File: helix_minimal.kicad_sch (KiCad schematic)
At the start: 18 parts, among them J1 USB-C, J2 WIZ850io J1, J3 WIZ850io J2, J4 3V3 microSD SPI breakout, J5 SWD, U1 STM32C071FBP6, U2 AP2112K-3.3

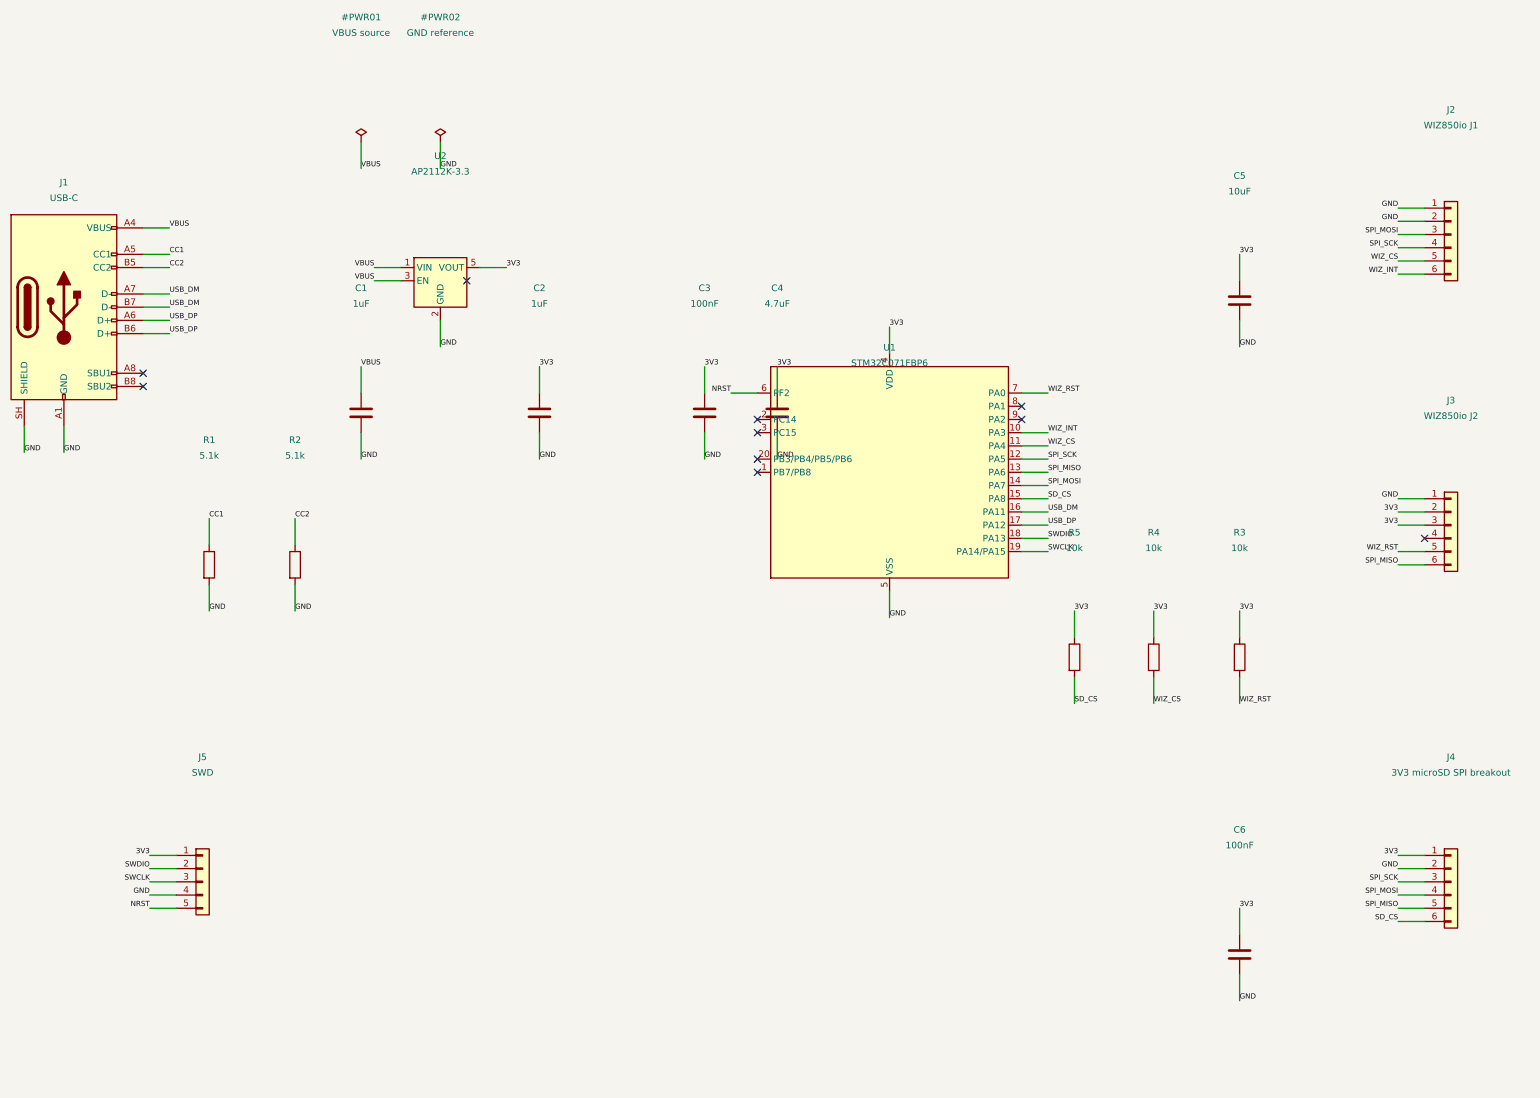
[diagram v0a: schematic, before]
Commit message: Add protected buck supply and switched peripheral rail
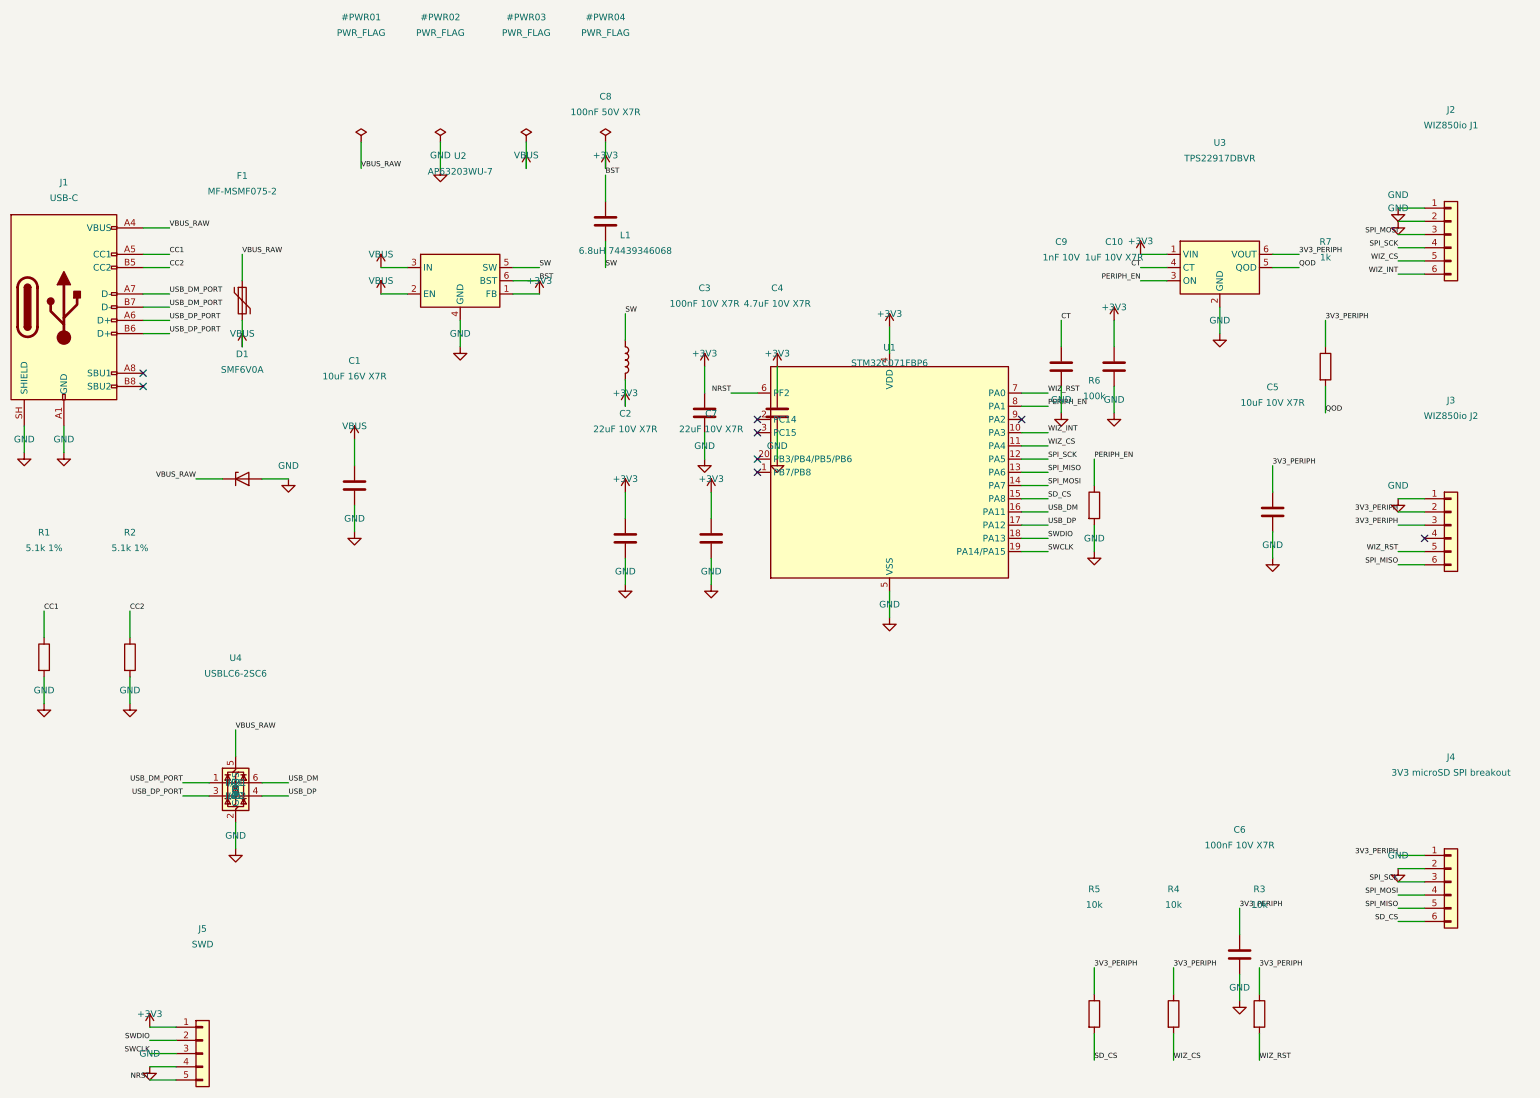
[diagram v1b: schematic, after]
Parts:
- added C10: 1uF 10V X7R, Capacitor_SMD:C_0603_1608Metric, symbol Device:C
- added C7: 22uF 10V X7R, Capacitor_SMD:C_1206_3216Metric, symbol Device:C
- added C8: 100nF 50V X7R, Capacitor_SMD:C_0603_1608Metric, symbol Device:C
- added C9: 1nF 10V, Capacitor_SMD:C_0603_1608Metric, symbol Device:C
- added D1: SMF6V0A, Diode_SMD:D_SMF, symbol Device:D_Zener
- added F1: MF-MSMF075-2, Fuse:Fuse_1812_4532Metric, symbol Device:Polyfuse
- added L1: 6.8uH 74439346068, Inductor_SMD:L_Wuerth_XHMI-6060, symbol Device:L
- added R6: 100k, Resistor_SMD:R_0603_1608Metric, symbol Device:R
- added R7: 1k, Resistor_SMD:R_0603_1608Metric, symbol Device:R
- added U3: TPS22917DBVR, Package_TO_SOT_SMD:SOT-23-6, symbol Power_Management:TPS22917DBV
- added U4: USBLC6-2SC6, Package_TO_SOT_SMD:SOT-23-6, symbol Power_Protection:USBLC6-2SC6
- C1: value 1uF -> 10uF 16V X7R; footprint Capacitor_SMD:C_0603_1608Metric -> Capacitor_SMD:C_1206_3216Metric
- C2: value 1uF -> 22uF 10V X7R; footprint Capacitor_SMD:C_0603_1608Metric -> Capacitor_SMD:C_1206_3216Metric
- C3, C6: value 100nF -> 100nF 10V X7R
- C4: value 4.7uF -> 4.7uF 10V X7R
- C5: value 10uF -> 10uF 10V X7R; footprint Capacitor_SMD:C_0805_2012Metric -> Capacitor_SMD:C_1206_3216Metric
- R1, R2: value 5.1k -> 5.1k 1%
- U2: value AP2112K-3.3 -> AP63203WU-7; footprint Package_TO_SOT_SMD:SOT-23-5 -> Package_TO_SOT_SMD:TSOT-23-6; symbol Helix:AP2112K-3.3 -> Regulator_Switching:AP63203WU
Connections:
- net GND: now also U2.4 (GND), C10.2, C7.2, C9.2, D1.2 (A), R6.2, U3.2 (GND), U4.2 (GND); no longer U2.2 (GND)
- net USB_DM: now also U4.6 (I/O1); no longer J1.A7 (D-), J1.B7 (D-)
- net USB_DP: now also U4.4 (I/O2); no longer J1.A6 (D+), J1.B6 (D+)
- net VBUS: now also U2.2 (EN), F1.2; no longer J1.A4 (VBUS), J1.A9 (VBUS), J1.B4 (VBUS), J1.B9 (VBUS), U2.1 (VIN)
- net PERIPH_EN: now reaches U1.8 (PA1)
- net PERIPH_EN: now also R6.1, U3.3 (ON)
- net 3V3 renamed 3V3_PERIPH
- net 3V3_PERIPH: now also R7.1, U3.6 (VOUT); no longer C2.1, C3.1, C4.1, J5.1 (Pin_1), U1.4 (VDD), U2.5 (VOUT)
- new net +3V3: C10.1, C2.1, C3.1, C4.1, C7.1, J5.1 (Pin_1), L1.2, U1.4 (VDD), U2.1 (FB), U3.1 (VIN)
- new net BST: C8.1, U2.6 (BST)
- new net CT: C9.1, U3.4 (CT)
- new net QOD: R7.2, U3.5 (QOD)
- new net SW: C8.2, L1.1, U2.5 (SW)
- new net USB_DM_PORT: J1.A7 (D-), J1.B7 (D-), U4.1 (I/O1)
- new net USB_DP_PORT: J1.A6 (D+), J1.B6 (D+), U4.3 (I/O2)
- new net VBUS_RAW: D1.1 (K), F1.1, J1.A4 (VBUS), J1.A9 (VBUS), J1.B4 (VBUS), J1.B9 (VBUS), U4.5 (VBUS)
- no-connect marks 10 -> 8
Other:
- moved on the sheet: C1, C2, C5, J5, R1, R2, R3, R4, R5

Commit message: Simplify power wiring to explicit supply symbols
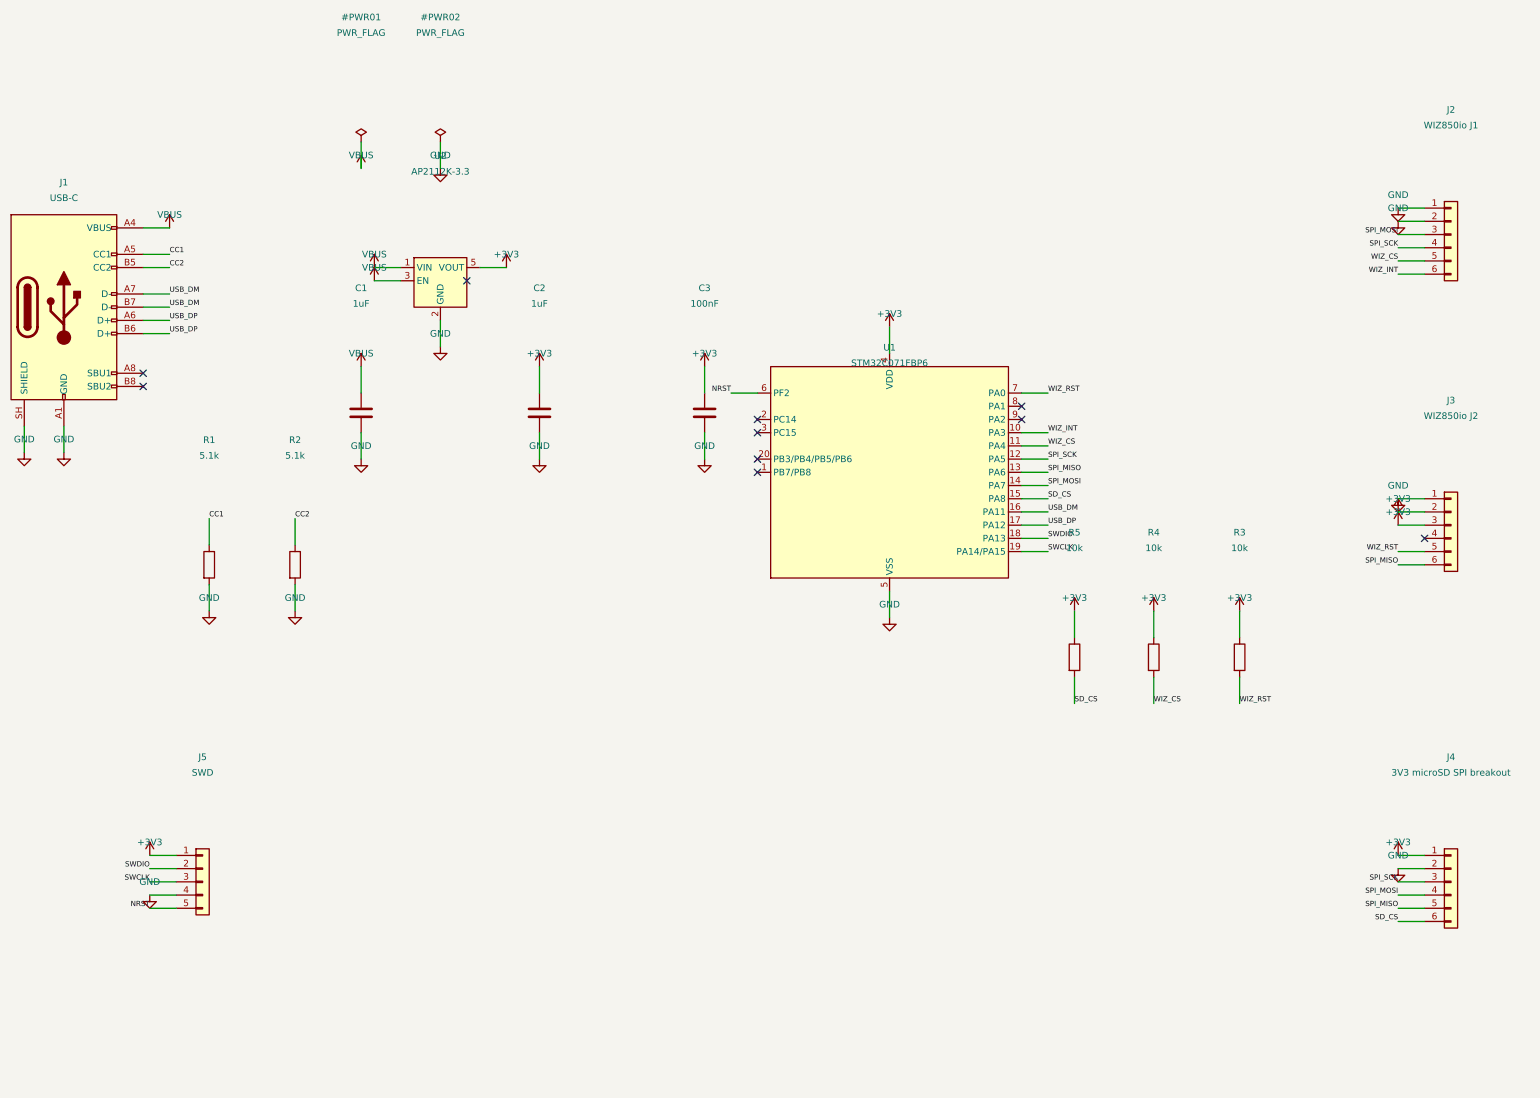
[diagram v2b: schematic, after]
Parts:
- removed C10: 1uF 10V X7R, Capacitor_SMD:C_0603_1608Metric, symbol Device:C
- removed C4: 4.7uF 10V X7R, Capacitor_SMD:C_0603_1608Metric, symbol Device:C
- removed C5: 10uF 10V X7R, Capacitor_SMD:C_1206_3216Metric, symbol Device:C
- removed C6: 100nF 10V X7R, Capacitor_SMD:C_0603_1608Metric, symbol Device:C
- removed C7: 22uF 10V X7R, Capacitor_SMD:C_1206_3216Metric, symbol Device:C
- removed C8: 100nF 50V X7R, Capacitor_SMD:C_0603_1608Metric, symbol Device:C
- removed C9: 1nF 10V, Capacitor_SMD:C_0603_1608Metric, symbol Device:C
- removed D1: SMF6V0A, Diode_SMD:D_SMF, symbol Device:D_Zener
- removed F1: MF-MSMF075-2, Fuse:Fuse_1812_4532Metric, symbol Device:Polyfuse
- removed L1: 6.8uH 74439346068, Inductor_SMD:L_Wuerth_XHMI-6060, symbol Device:L
- removed R6: 100k, Resistor_SMD:R_0603_1608Metric, symbol Device:R
- removed R7: 1k, Resistor_SMD:R_0603_1608Metric, symbol Device:R
- removed U3: TPS22917DBVR, Package_TO_SOT_SMD:SOT-23-6, symbol Power_Management:TPS22917DBV
- removed U4: USBLC6-2SC6, Package_TO_SOT_SMD:SOT-23-6, symbol Power_Protection:USBLC6-2SC6
- C1: value 10uF 16V X7R -> 1uF; footprint Capacitor_SMD:C_1206_3216Metric -> Capacitor_SMD:C_0603_1608Metric
- C2: value 22uF 10V X7R -> 1uF; footprint Capacitor_SMD:C_1206_3216Metric -> Capacitor_SMD:C_0603_1608Metric
- C3: value 100nF 10V X7R -> 100nF
- R1, R2: value 5.1k 1% -> 5.1k
- U2: value AP63203WU-7 -> AP2112K-3.3; footprint Package_TO_SOT_SMD:TSOT-23-6 -> Package_TO_SOT_SMD:SOT-23-5; symbol Regulator_Switching:AP63203WU -> Helix:AP2112K-3.3
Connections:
- net 3V3_PERIPH is gone; now on net +3V3: J3.2 (Pin_2), J3.3 (Pin_3), J4.1 (Pin_1), R3.1, R4.1, R5.1
- net SW is gone; now on net +3V3: U2.5 (VOUT)
- net USB_DM_PORT is gone; now on net USB_DM: J1.A7 (D-), J1.B7 (D-)
- net USB_DP_PORT is gone; now on net USB_DP: J1.A6 (D+), J1.B6 (D+)
- net VBUS_RAW is gone; now on net VBUS: J1.A4 (VBUS), J1.A9 (VBUS), J1.B4 (VBUS), J1.B9 (VBUS)
- net +3V3: no longer U2.1 (FB)
- net GND: now also U2.2 (GND); no longer U2.4 (GND)
- net VBUS: now also U2.1 (VIN); no longer U2.2 (EN)
- removed net BST: U2.6 (BST)
- net PERIPH_EN: no longer names the net of U1.8 (PA1)
- no-connect marks 8 -> 10
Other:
- moved on the sheet: C1, C2, J5, R1, R2, R3, R4, R5
